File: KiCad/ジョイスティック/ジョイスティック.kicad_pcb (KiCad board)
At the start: 2 copper layers, 1 part

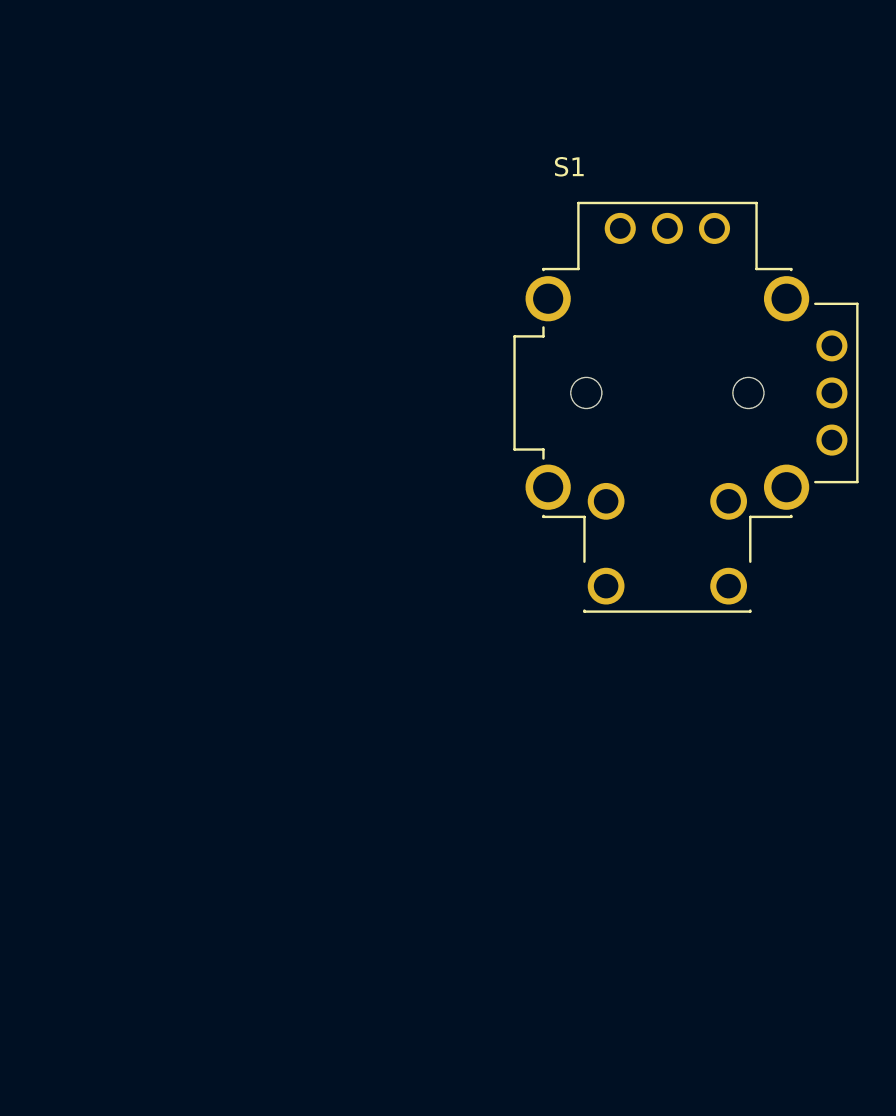
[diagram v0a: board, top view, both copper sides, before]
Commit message: wip シールドを介してGNDがつながってる
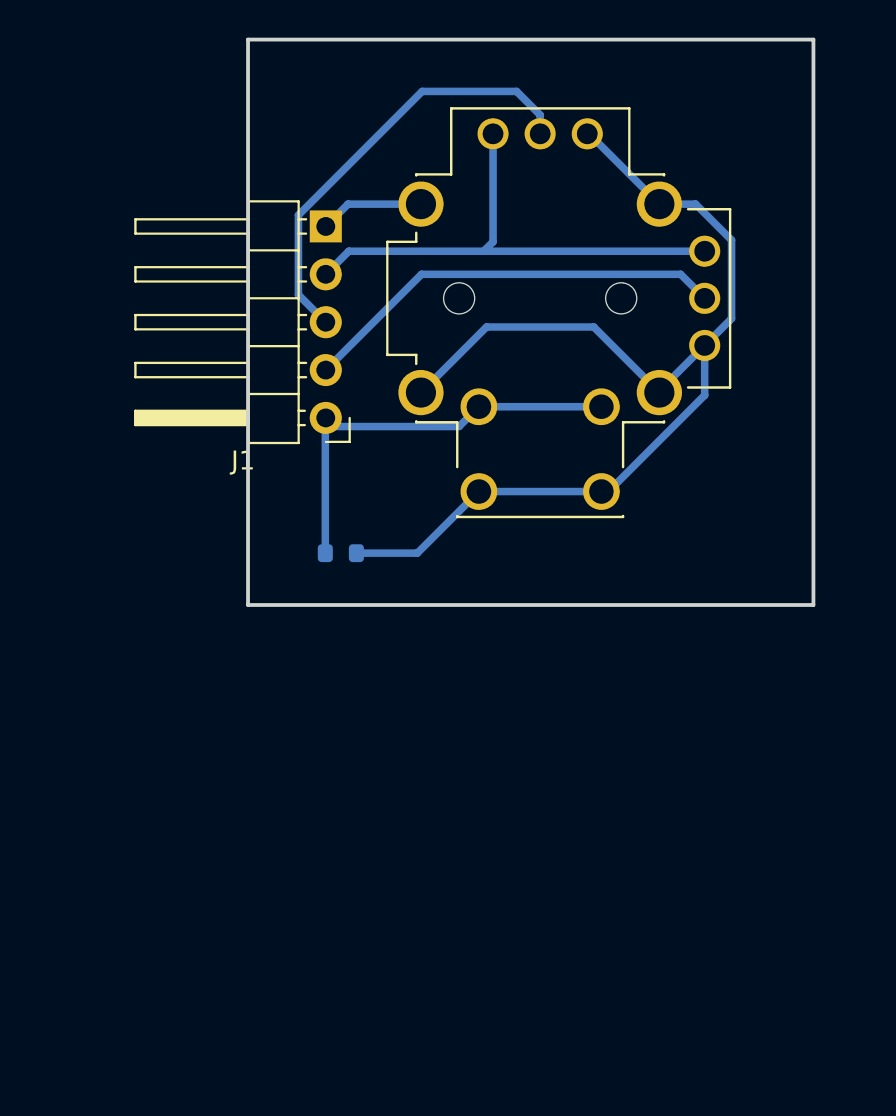
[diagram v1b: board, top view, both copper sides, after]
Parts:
- added J1: Conn_01x05_Pin, Connector_PinHeader_2.54mm:PinHeader_1x05_P2.54mm_Horizontal, F.Cu at (114.1, 100.1)
- added R1: 10k, Resistor_SMD:R_0603_1608Metric, B.Cu at (114.9, 107.2)
- moved S1 8.41 mm to (125.5, 93.7)
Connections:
- S1 pad A: unconnected-(S1-PadA) -> /SW
- S1 pad B: unconnected-(S1-PadB) -> GND
- S1 pad C: unconnected-(S1-PadC) -> /SW
- S1 pad D: unconnected-(S1-PadD) -> GND
- S1 pad VR1_1: (no net) -> GND
- S1 pad VR1_2: (no net) -> /VR1
- S1 pad VR1_3: (no net) -> /Vin
- S1 pad VR2_1: (no net) -> GND
- S1 pad VR2_2: (no net) -> /VR2
- S1 pad VR2_3: (no net) -> /Vin
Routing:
- net GND: track 0.00 -> 65.2 mm
- net /Vin: track 0.00 -> 27.0 mm
- net /VR2: track 0.00 -> 23.3 mm
- net /VR1: track 0.00 -> 22.7 mm
- net /SW: track 0.00 -> 22.4 mm
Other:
- board outline added: 30 x 30 mm

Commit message: 多分全部つながった
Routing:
- net GND: track 65.2 -> 87.0 mm, vias 0 -> 2
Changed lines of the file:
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@@
+	)
+	(segment
+		(start 130.574 83.574)
+		(end 120.426 83.574)
+		(width 0.4)
+		(layer "F.Cu")
+		(net 5)
+	)
+	(segment
+		(start 132 85)
+		(end 130.574 83.574)
+		(width 0.4)
+		(layer "F.Cu")
+		(net 5)
+	)
+	(segment
+		(start 120.426 83.574)
+		(end 119 85)
+		(width 0.4)
+		(layer "F.Cu")
+		(net 5)
+	)
+	(via
+		(at 119 85)
+		(size 1.6)
+		(drill 1)
+		(layers "F.Cu" "B.Cu")
+		(free yes)
+		(net 5)
+	)
+	(via
+		(at 132 85)
+		(size 1.6)
+		(drill 1)
+		(layers "F.Cu" "B.Cu")
+		(free yes)
+		(net 5)
 	)
 	(segment
 		(start 135.656 90.639331)
 		(end 133.746669 88.73)
+		(width 0.4)
+		(layer "B.Cu")
+		(net 5)
+	)
+	(segment
+		(start 119 85)
+		(end 119 88.555)
 		(width 0.4)
 		(layer "B.Cu")
@@
 		(start 122.25 103.98)
 		(end 128.75 103.98)
+		(width 0.4)
+		(layer "B.Cu")
+		(net 5)
+	)
+	(segment
+		(start 132 85)
+		(end 132 88.555)
 		(width 0.4)
 		(layer "B.Cu")
@@
 		(width 0.4)
 		(layer "B.Cu")
+		(net 5)
+	)
+	(segment
+		(start 132 88.555)
+		(end 131.825 88.73)
+		(width 0.4)
+		(layer "B.Cu")
+		(net 5)
+	)
+	(segment
+		(start 119 88.555)
+		(end 119.175 88.73)
+		(width 0.4)
+		(layer "B.Cu")

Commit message: 暫定版
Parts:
- moved R1 3.17 mm to (116.5, 104.5), turned to -90 degrees
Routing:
- net /SW: track 22.4 -> 19.9 mm
- net GND: track 87.0 -> 85.5 mm
- added copper zone on B.Cu, net GND
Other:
- outline, holes or cut-outs redrawn
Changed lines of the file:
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@@
 			(outputformat 1)
 			(mirror no)
-			(drillshape 1)
+			(drillshape 0)
 			(scaleselection 1)
 			(outputdirectory "")
@@
 			(at -6.325 -5)
 			(size 2.4 2.4)
-			(drill 1.6)
+			(drill 1)
 			(layers "*.Cu" "*.Mask")
 			(remove_unused_layers no)
@@
 			(at 6.325 -5)
 			(size 2.4 2.4)
-			(drill 1.6)
+			(drill 1)
 			(layers "*.Cu" "*.Mask")
 			(remove_unused_layers no)
@@
 			(at 6.325 5)
 			(size 2.4 2.4)
-			(drill 1.6)
+			(drill 1)
 			(layers "*.Cu" "*.Mask")
 			(remove_unused_layers no)
@@
 			(at -6.325 5)
 			(size 2.4 2.4)
-			(drill 1.6)
+			(drill 1)
 			(layers "*.Cu" "*.Mask")
 			(remove_unused_layers no)
@@
 		)
 		(embedded_fonts no)
+		(model "C:/Users/Ryunosuke/Desktop/RKJXV122400R--3DModel-STEP-805722.STEP"
+			(offset
+				(xyz 0 0 0)
+			)
+			(scale
+				(xyz 1 1 1)
+			)
+			(rotate
+				(xyz -0 -0 -180)
+			)
+		)
 	)
 	(footprint "Resistor_SMD:R_0603_1608Metric"
 		(layer "B.Cu")
-		(at 114.925 107.25)
+		(at 116.5 104.5 -90)
 		(descr "Resistor SMD 0603 (1608 Metric), square (rectangular) end terminal, IPC_7351 nominal, (Body size source: IPC-SM-782 page 72, https://www.pcb-3d.com/wordpress/wp-content/uploads/ipc-sm-782a_amendment_1_and_2.pdf), generated with kicad-footprint-generator")
 		(tags "resistor")
 		(property "Reference" "R1"
-			(at 0 1.43 0)
+			(at 0 1.43 90)
 			(layer "B.SilkS")
 			(effects
@@
 		)
 		(property "Value" "10k"
-			(at -0.075 -1.43 0)
+			(at -0.075 -1.43 90)
 			(layer "B.Fab")
 			(effects
@@
 		)
 		(property "Datasheet" ""
-			(at 0 0 180)
+			(at 0 0 90)
 			(unlocked yes)
 			(layer "B.Fab")
@@
 		)
 		(property "Description" "Resistor"
-			(at 0 0 180)
+			(at 0 0 90)
 			(unlocked yes)
 			(layer "B.Fab")
@@
 		(attr smd)
 		(fp_line
+			(start -0.237258 0.5225)
+			(end 0.237258 0.5225)
+			(stroke
+				(width 0.12)
+				(type solid)
+			)
+			(layer "B.SilkS")
+		)
+		(fp_line
 			(start -0.237258 -0.5225)
 			(end 0.237258 -0.5225)
@@
 		)
 		(fp_line
-			(start -0.237258 0.5225)
-			(end 0.237258 0.5225)
-			(stroke
-				(width 0.12)
-				(type solid)
-			)
-			(layer "B.SilkS")
+			(start -1.48 0.73)
+			(end 1.48 0.73)
+			(stroke
+				(width 0.05)
+				(type solid)
+			)
+			(layer "B.CrtYd")
+		)
+		(fp_line
+			(start 1.48 0.73)
+			(end 1.48 -0.73)
+			(stroke
+				(width 0.05)
+				(type solid)
+			)
+			(layer "B.CrtYd")
 		)
 		(fp_line
@@
 		)
 		(fp_line
-			(start -1.48 0.73)
-			(end 1.48 0.73)
-			(stroke
-				(width 0.05)
-				(type solid)
-			)
-			(layer "B.CrtYd")
-		)
-		(fp_line
 			(start 1.48 -0.73)
 			(end -1.48 -0.73)
@@
 		)
 		(fp_line
-			(start 1.48 0.73)
-			(end 1.48 -0.73)
-			(stroke
-				(width 0.05)
-				(type solid)
-			)
-			(layer "B.CrtYd")
+			(start -0.8 0.4125)
+			(end 0.8 0.4125)
+			(stroke
+				(width 0.1)
+				(type solid)
+			)
+			(layer "B.Fab")
+		)
+		(fp_line
+			(start 0.8 0.4125)
+			(end 0.8 -0.4125)
+			(stroke
+				(width 0.1)
+				(type solid)
+			)
+			(layer "B.Fab")
 		)
 		(fp_line
@@
 		)
 		(fp_line
-			(start -0.8 0.4125)
-			(end 0.8 0.4125)
-			(stroke
-				(width 0.1)
-				(type solid)
-			)
-			(layer "B.Fab")
-		)
-		(fp_line
 			(start 0.8 -0.4125)
 			(end -0.8 -0.4125)
@@
 			(layer "B.Fab")
 		)
-		(fp_line
-			(start 0.8 0.4125)
-			(end 0.8 -0.4125)
-			(stroke
-				(width 0.1)
-				(type solid)
-			)
-			(layer "B.Fab")
-		)
 		(fp_text user "${REFERENCE}"
-			(at 0 0 0)
+			(at 0 0 90)
 			(layer "B.Fab")
 			(effects
@@
 		)
 		(pad "1" smd roundrect
-			(at -0.825 0)
+			(at -0.825 0 270)
 			(size 0.8 0.95)
 			(layers "B.Cu" "B.Mask" "B.Paste")
@@
 		)
 		(pad "2" smd roundrect
-			(at 0.825 0)
+			(at 0.825 0 270)
 			(size 0.8 0.95)
 			(layers "B.Cu" "B.Mask" "B.Paste")
@@
 			)
 		)
+	)
+	(gr_circle
+		(center 112.5 107.5)
+		(end 112.5 106.5)
+		(stroke
+			(width 0.05)
+			(type default)
+		)
+		(fill no)
+		(layer "Edge.Cuts")
+	)
+	(gr_circle
+		(center 112.5 82.5)
+		(end 112.5 81.5)
+		(stroke
+			(width 0.05)
+			(type default)
+		)
+		(fill no)
+		(layer "Edge.Cuts")
+	)
+	(gr_circle
+		(center 137.5 107.5)
+		(end 137.5 106.5)
+		(stroke
+			(width 0.05)
+			(type default)
+		)
+		(fill no)
+		(layer "Edge.Cuts")
 	)
 	(gr_rect
@@
 		(layer "Edge.Cuts")
 	)
+	(gr_circle
+		(center 137.5 82.5)
+		(end 137.5 81.5)
+		(stroke
+			(width 0.05)
+			(type default)
+		)
+		(fill no)
+		(layer "Edge.Cuts")
+	)
+	(segment
+		(start 114.125 100.075)
+		(end 116.5 102.45)
+		(width 0.4)
+		(layer "B.Cu")
+		(net 1)
+	)
 	(segment
 		(start 114.1 100.1)
@@
 	)
 	(segment
-		(start 114.1 107.25)
-		(end 114.1 100.1)
-		(width 0.4)
-		(layer "B.Cu")
-		(net 1)
-	)
-	(segment
 		(start 121.199 100.531)
 		(end 114.581 100.531)
@@
 		(start 122.25 99.48)
 		(end 121.199 100.531)
+		(width 0.4)
+		(layer "B.Cu")
+		(net 1)
+	)
+	(segment
+		(start 116.5 102.45)
+		(end 116.5 103.675)
 		(width 0.4)
 		(layer "B.Cu")
@@
 	)
 	(segment
+		(start 120.73 105.5)
+		(end 122.25 103.98)
+		(width 0.4)
+		(layer "B.Cu")
+		(net 5)
+	)
+	(segment
 		(start 133.746669 88.73)
 		(end 131.825 88.73)
@@
 	)
 	(segment
-		(start 122.25 103.98)
-		(end 118.98 107.25)
-		(width 0.4)
-		(layer "B.Cu")
-		(net 5)
-	)
-	(segment
 		(start 131.825 88.73)
 		(end 128.095 85)
@@
 	)
 	(segment
+		(start 116.575 105.5)
+		(end 120.73 105.5)
+		(width 0.4)
+		(layer "B.Cu")
+		(net 5)
+	)
+	(segment
 		(start 132 88.555)
 		(end 131.825 88.73)
@@
 	)
 	(segment
-		(start 118.98 107.25)
-		(end 115.75 107.25)
-		(width 0.4)
-		(layer "B.Cu")
-		(net 5)
-	)
-	(segment
 		(start 135.656 94.804)
 		(end 135.656 90.639331)
@@
 		(net 5)
 	)
+	(zone
+		(net 5)
+		(net_name "GND")
+		(layer "B.Cu")
+		(hatch edge 0.5)
+		(connect_pads
+			(clearance 0.5)
+		)
+		(min_thickness 0.25)
+		(filled_areas_thickness no)
+		(fill yes
+			(thermal_gap 0.5)
+			(thermal_bridge_width 0.5)
+		)
+		(polygon
+			(pts
+				(xy 140 80) (xy 110 80) (xy 110 110) (xy 140 110)
+			)
+		)
+	)
 	(embedded_fonts no)

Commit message: バカの配線を破壊
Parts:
- moved R1 27.1 mm to (127.2, 129.4), turned to 90 degrees
- moved S1 26.8 mm to (120.0, 120.0)
- moved J1 25.4 mm to (109.0, 125.0)
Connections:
- R1 pad 2: GND -> /Vin
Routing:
- net GND: track 85.5 -> 0.00 mm
- net /Vin: track 27.0 -> 0.00 mm
- net /VR2: track 23.3 -> 0.00 mm
- net /VR1: track 22.7 -> 0.00 mm
- net /SW: track 19.9 -> 0.00 mm
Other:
- outline, holes or cut-outs redrawn
